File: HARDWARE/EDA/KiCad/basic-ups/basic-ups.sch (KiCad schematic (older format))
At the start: 10 parts

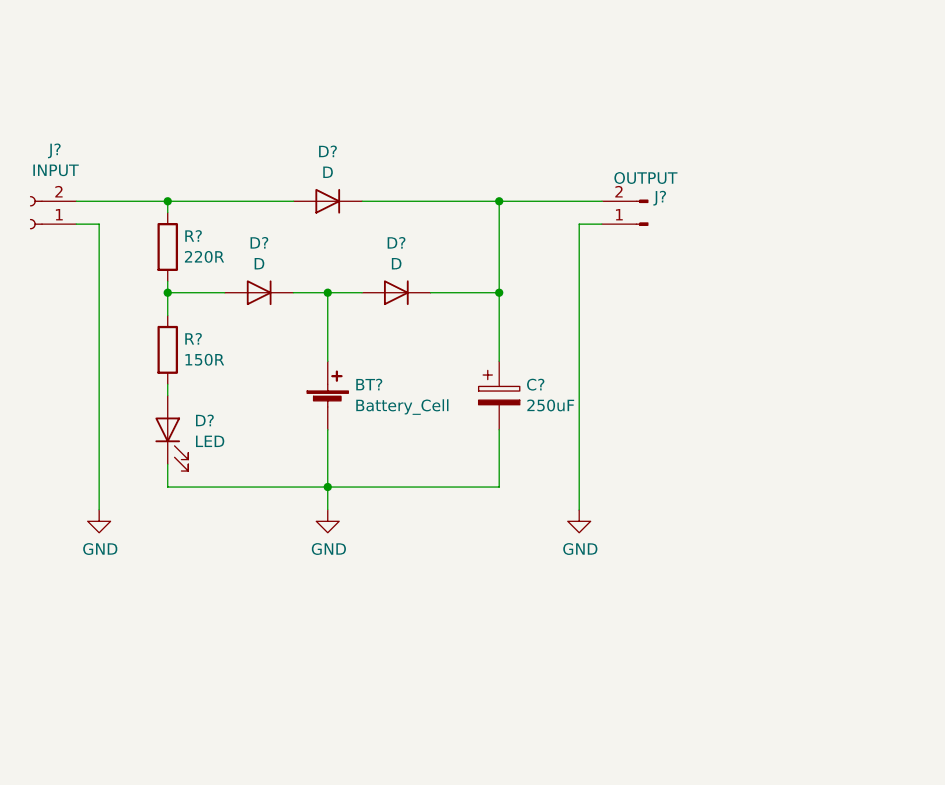
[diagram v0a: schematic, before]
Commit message: schematic elaborated
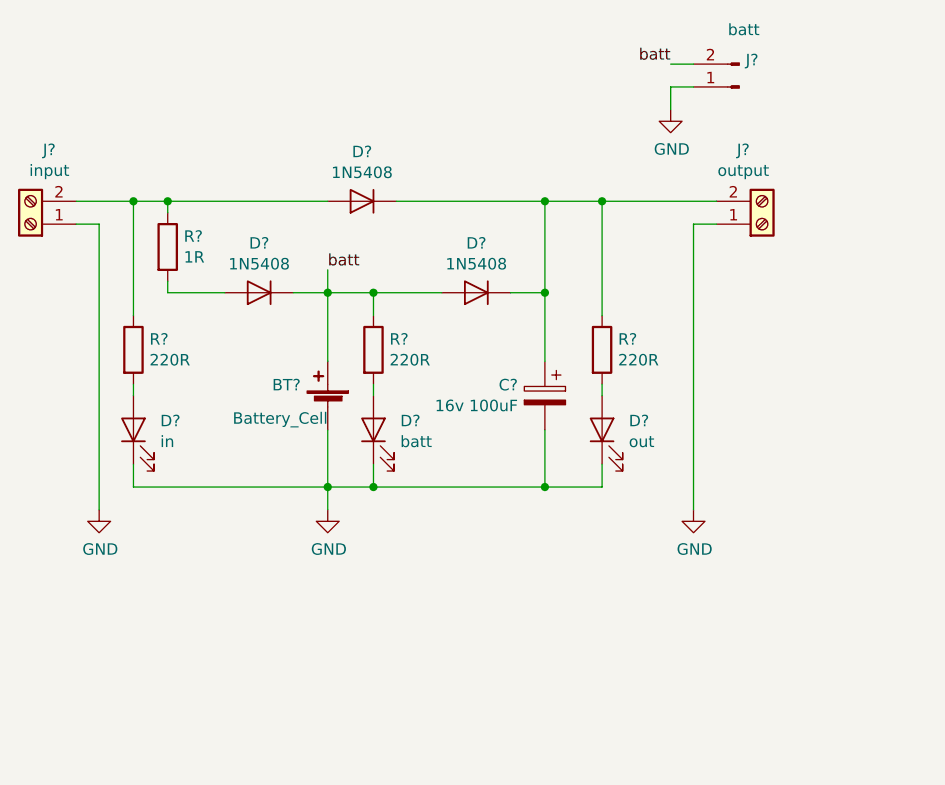
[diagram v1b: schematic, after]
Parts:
- removed D? (x3): D, symbol Device:D
- removed J?: OUTPUT, symbol Connector:Conn_01x02_Male
- removed J?: INPUT, symbol Connector:Conn_01x02_Female
- added D? (x3): 1N5408, Diode_THT:D_DO-201AD_P15.24mm_Horizontal, symbol Diode:1N5408
- added D?: batt, LED_THT:LED_D5.0mm, symbol Device:LED
- added D?: out, LED_THT:LED_D5.0mm, symbol Device:LED
- added J?: input, Connector_Phoenix_MC:PhoenixContact_MC_1,5_2-G-3.81_1x02_P3.81mm_Horizontal, symbol Connector:Screw_Terminal_01x02
- added J?: output, Connector_Phoenix_MC:PhoenixContact_MC_1,5_2-G-3.81_1x02_P3.81mm_Horizontal, symbol Connector:Screw_Terminal_01x02
- added J?: batt, Connector_PinHeader_2.54mm:PinHeader_1x02_P2.54mm_Horizontal, symbol Connector:Conn_01x02_Male
- added R? (x2): 220R, Resistor_THT:R_Axial_DIN0207_L6.3mm_D2.5mm_P7.62mm_Horizontal, symbol Device:R
- BT?: footprint (none) -> Connector_AMASS:AMASS_XT30UPB-F_1x02_P5.0mm_Vertical
- C?: value 250uF -> 16v 100uF; footprint (none) -> Capacitor_THT:CP_Radial_D6.3mm_P2.50mm
- D?: value LED -> in; footprint (none) -> LED_THT:LED_D5.0mm
- R?: value 220R -> 1R; footprint (none) -> Resistor_THT:R_Axial_DIN0207_L6.3mm_D2.5mm_P7.62mm_Horizontal
- R?: value 150R -> 220R; footprint (none) -> Resistor_THT:R_Axial_DIN0207_L6.3mm_D2.5mm_P7.62mm_Horizontal
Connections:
- net GND: now also D?.1 (K), D?.1 (K), J?.1 (Pin_1), J?.1 (Pin_1), J?.1 (Pin_1)
- net batt: now reaches BT?.1 (+)
- net batt: now also D?.1 (K), D?.2 (A), J?.2 (Pin_2), R?.1
- net at R?.1: now also R?.1, D?.2 (A), J?.2 (Pin_2); no longer R?.2
- net at C?.1: now also D?.1 (K), D?.1 (K), J?.2 (Pin_2), R?.1
- new net: D?.2 (A), R?.2 (x3)
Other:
- moved on the sheet: C?, D?, R?

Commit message: finished project
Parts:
- removed D? (x3): 1N5408, Diode_THT:D_DO-201AD_P15.24mm_Horizontal, symbol Diode:1N5408
- added D2, D3, D5: 1N5400, Diode_THT:D_DO-201AD_P15.24mm_Horizontal, symbol Diode:1N5400
- added J4: batt, Connector_Phoenix_MC:PhoenixContact_MC_1,5_2-G-3.81_1x02_P3.81mm_Horizontal, symbol Connector:Screw_Terminal_01x02
- BT1: renamed from BT?; footprint Connector_AMASS:AMASS_XT30UPB-F_1x02_P5.0mm_Vertical -> (none)
- J2: renamed from J?; footprint Connector_PinHeader_2.54mm:PinHeader_1x02_P2.54mm_Horizontal -> Connector_JST:JST_EH_S2B-EH_1x02_P2.50mm_Horizontal
- R2: renamed from R?; value 1R -> 220R
- gave numbers to parts that had none: 9
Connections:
- net GND: now also J4.1 (Pin_1)
- net batt: now also D2.1 (K), D5.2 (A), J4.2 (Pin_2)
- net at J1.2 (Pin_2), R1.1, R2.1: now also D3.2 (A)
- net at R2.2: now also D2.2 (A)
- net at C1.1, J3.2 (Pin_2), R4.1: now also D3.1 (K), D5.1 (K)
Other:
- moved on the sheet: BT1, C1, D1, D4, D6, J1, J2, J3, R1, R2, R3, R4
